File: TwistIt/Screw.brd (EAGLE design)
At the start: 33.5 x 36.5 mm, 8 parts

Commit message: Minor fixes everywhere
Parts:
- R1, R2, R3: value (none) -> 330
- ST1: value 5PIN_SCREW -> (none)
- renumbered U$1 to APM, U$2 to ST1
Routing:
- net VCC: track 16.5 -> 15.3 mm
- net P1: track 20.5 -> 19.7 mm
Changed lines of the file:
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@@
 <elements>
 <element name="JP1" library="jumper" package="JP1" value="" x="22.11928125" y="31.597309375"/>
-<element name="R1" library="resistor" package="R0603" value="" x="25.66984375" y="32.243665625" rot="R90"/>
-<element name="R2" library="resistor" package="R0603" value="" x="28.647703125" y="32.22621875" rot="R90"/>
-<element name="R3" library="resistor" package="R0603" value="" x="31.33979375" y="32.273709375" rot="R90"/>
-<element name="U$1" library="pie" package="ARDUINO_PRO_MICRO" value="ARDUINO_PRO_MICRO" x="1.778" y="1.778"/>
-<element name="U$2" library="pie" package="5PIN_SCREW" value="5PIN_SCREW" x="28.783865625" y="28.3851625" rot="MR270"/>
+<element name="R1" library="resistor" package="R0603" value="330" x="25.66984375" y="32.243665625" rot="R90"/>
+<element name="R2" library="resistor" package="R0603" value="330" x="28.647703125" y="32.22621875" rot="R90"/>
+<element name="R3" library="resistor" package="R0603" value="330" x="31.33979375" y="32.273709375" rot="R90"/>
+<element name="APM" library="pie" package="ARDUINO_PRO_MICRO" value="ARDUINO_PRO_MICRO" x="1.778" y="1.778"/>
+<element name="ST1" library="pie" package="5PIN_SCREW" value="" x="28.783865625" y="28.3851625" rot="MR270"/>
 <element name="U$3" library="pie" package="PIE-LOGO-SMALL" value="" x="5.842" y="27.94" rot="MR0"/>
 <element name="U$4" library="pie" package="OSHW-LOGO-S" value="" x="3.302" y="33.782" rot="MR0"/>
@@
 </signal>
 <signal name="GND">
-<contactref element="U$1" pad="GND@0"/>
+<contactref element="APM" pad="GND@0"/>
 <polygon width="0.4064" layer="16">
 <vertex x="0.508" y="36.068"/>
@@
 <vertex x="33.02" y="36.068"/>
 </polygon>
-<contactref element="U$2" pad="P$5"/>
+<contactref element="ST1" pad="P$5"/>
 </signal>
 <signal name="VCC">
-<contactref element="U$2" pad="P$1"/>
+<contactref element="ST1" pad="P$1"/>
 <contactref element="JP1" pad="1"/>
-<contactref element="U$1" pad="VCC"/>
-<wire x1="18.288" y1="23.368" x2="22.11928125" y2="27.19928125" width="0.8128" layer="16"/>
+<contactref element="APM" pad="VCC"/>
+<wire x1="18.796" y1="23.876" x2="22.11928125" y2="27.19928125" width="0.8128" layer="16"/>
 <wire x1="22.11928125" y1="27.19928125" x2="22.11928125" y2="30.327309375" width="0.8128" layer="16"/>
 <wire x1="25.483865625" y1="25.2851625" x2="23.566703125" y2="23.368" width="0.8128" layer="16"/>
-<wire x1="23.566703125" y1="23.368" x2="18.288" y2="23.368" width="0.8128" layer="16"/>
+<wire x1="23.566703125" y1="23.368" x2="18.796" y2="23.876" width="0.8128" layer="16"/>
 </signal>
 <signal name="P1">
 <contactref element="R1" pad="1"/>
-<contactref element="U$2" pad="P$2"/>
-<contactref element="U$1" pad="A2"/>
-<wire x1="18.288" y1="18.288" x2="20.2851625" y2="20.2851625" width="0.4064" layer="1"/>
+<contactref element="ST1" pad="P$2"/>
+<contactref element="APM" pad="A2"/>
+<wire x1="18.796" y1="18.796" x2="20.2851625" y2="20.2851625" width="0.4064" layer="1"/>
 <wire x1="20.2851625" y1="20.2851625" x2="25.483865625" y2="20.2851625" width="0.4064" layer="1"/>
 <wire x1="25.483865625" y1="20.2851625" x2="27.178" y2="21.979296875" width="0.4064" layer="1"/>
@@
 </signal>
 <signal name="P2">
-<contactref element="U$2" pad="P$3"/>
-<contactref element="U$1" pad="A1"/>
+<contactref element="ST1" pad="P$3"/>
+<contactref element="APM" pad="A1"/>
 <contactref element="R2" pad="1"/>
 <wire x1="25.483865625" y1="15.2851625" x2="28.647703125" y2="18.449" width="0.4064" layer="1"/>
 <wire x1="28.647703125" y1="18.449" x2="28.647703125" y2="31.37621875" width="0.4064" layer="1"/>
 <wire x1="25.483865625" y1="15.2851625" x2="25.021028125" y2="15.748" width="0.4064" layer="1"/>
-<wire x1="25.021028125" y1="15.748" x2="18.288" y2="15.748" width="0.4064" layer="1"/>
+<wire x1="25.021028125" y1="15.748" x2="18.796" y2="16.256" width="0.4064" layer="1"/>
 </signal>
 <signal name="P3">
-<contactref element="U$2" pad="P$4"/>
-<contactref element="U$1" pad="A0"/>
+<contactref element="ST1" pad="P$4"/>
+<contactref element="APM" pad="A0"/>
 <contactref element="R3" pad="1"/>
 <wire x1="25.483865625" y1="10.2851625" x2="22.561028125" y2="13.208" width="0.4064" layer="1"/>
-<wire x1="22.561028125" y1="13.208" x2="18.288" y2="13.208" width="0.4064" layer="1"/>
+<wire x1="22.561028125" y1="13.208" x2="18.796" y2="13.716" width="0.4064" layer="1"/>
 <wire x1="25.483865625" y1="10.2851625" x2="31.33979375" y2="16.141090625" width="0.4064" layer="1"/>
 <wire x1="31.33979375" y1="16.141090625" x2="31.33979375" y2="31.423709375" width="0.4064" layer="1"/>

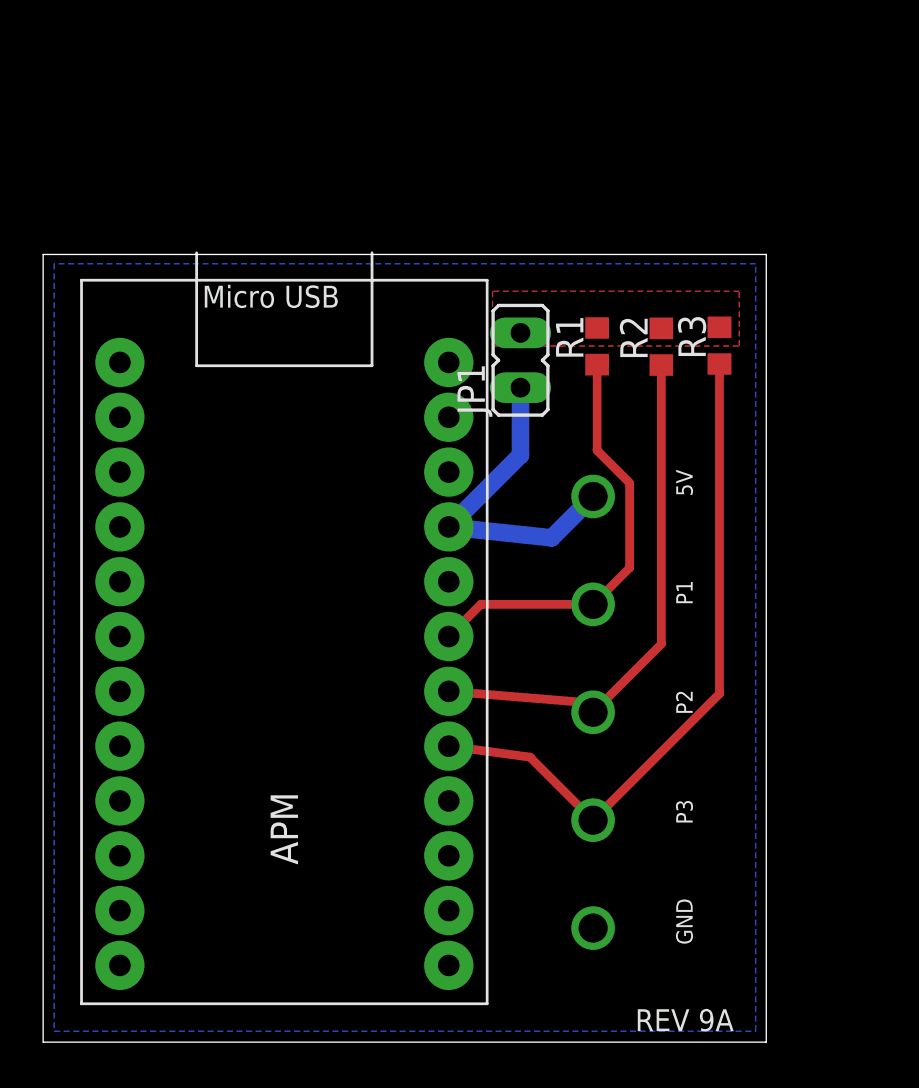
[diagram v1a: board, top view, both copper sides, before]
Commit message: Arrange TwistIt to be smaller with all components under arduino
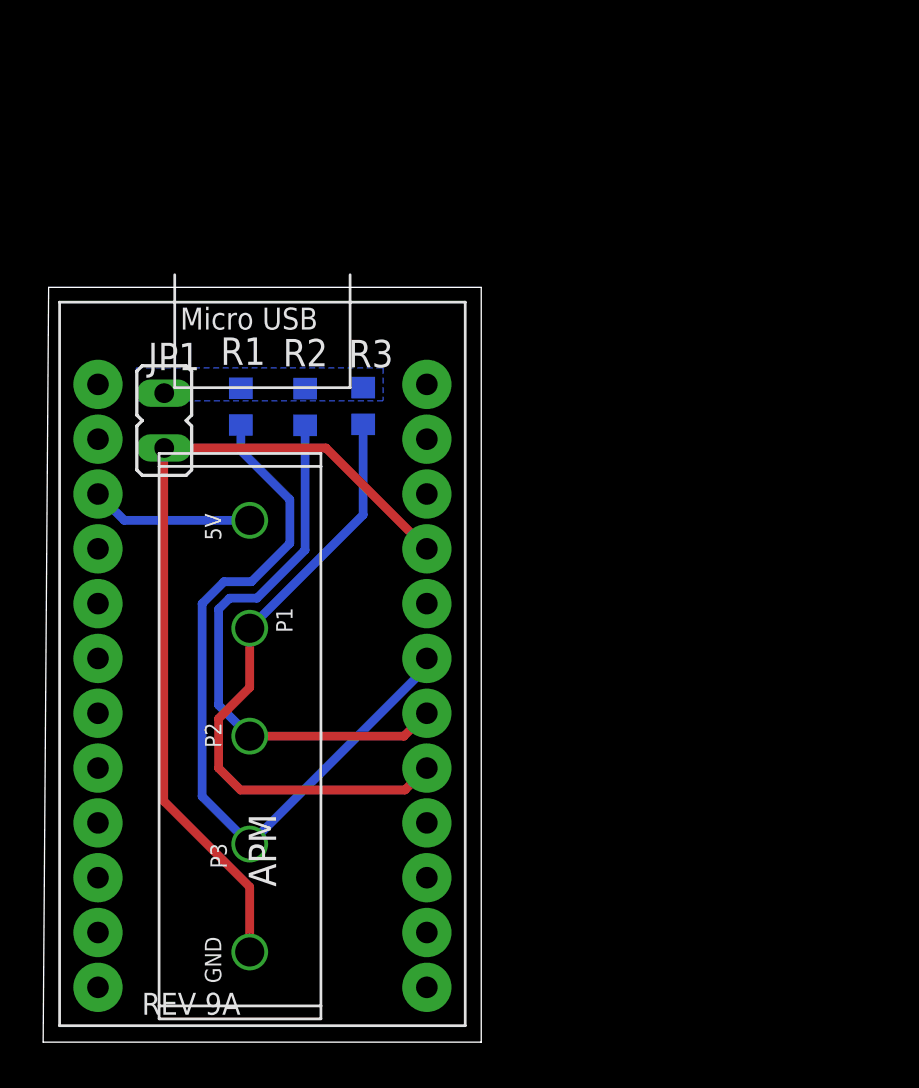
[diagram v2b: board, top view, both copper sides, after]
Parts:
- moved ST1 31.6 mm to (12.9, 1.08), flipped to the top, turned to 90 degrees
- moved JP1 16.7 mm to (5.61, 28.8)
- moved R1 16.7 mm to (9.16, 29.4), flipped to the bottom
- moved R2 16.7 mm to (12.1, 29.4), flipped to the bottom
- moved R3 16.7 mm to (14.8, 29.5), flipped to the bottom
- moved U$3 9.57 mm to (9.40, 19.1)
- moved APM 1.44 mm to (0.76, 0.76)
- moved U$4 1.44 mm to (2.29, 32.8)
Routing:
- net VCC: track 15.3 -> 39.1 mm
- net P1: track 19.7 -> 35.7 mm
- net GND: track 0.00 -> 7.54 mm
- net P3: track 31.5 -> 29.2 mm
- net P2: track 24.3 -> 26.1 mm
- added copper zone on layer 16, net 5V
- removed copper zone on layer 1, net 5V
- removed copper zone on layer 16, net GND
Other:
- board size 33.5 x 36.5 mm -> 20.3 x 35 mm

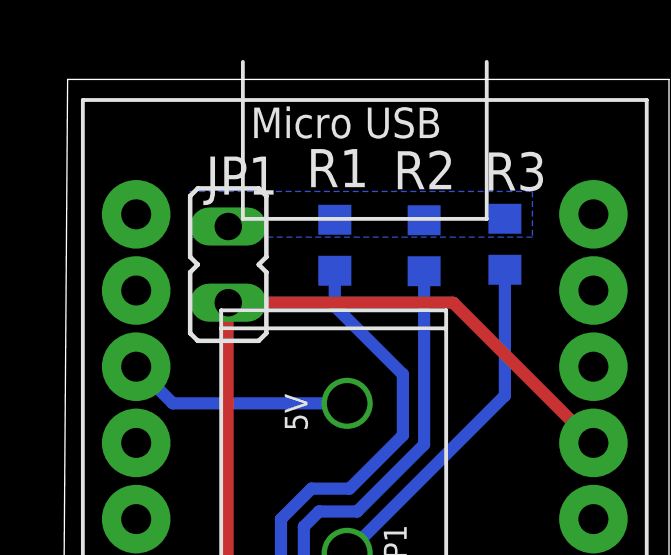
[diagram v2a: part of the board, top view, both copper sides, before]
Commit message: Mirror jumper in Screw.brd
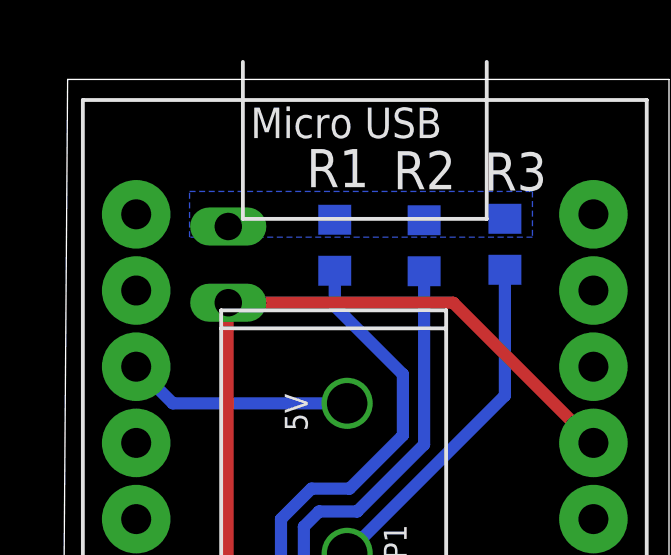
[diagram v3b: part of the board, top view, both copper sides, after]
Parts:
- flipped JP1 to the bottom
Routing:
- net VCC: vias 0 -> 1
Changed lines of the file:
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@@
 </autorouter>
 <elements>
-<element name="JP1" library="jumper" package="JP1" value="" x="5.60928125" y="28.803309375" smashed="yes">
-<attribute name="NAME" x="7.264690625" y="32.40628125" size="1.27" layer="25" font="vector" ratio="10" rot="R180"/>
-<attribute name="VALUE" x="8.53028125" y="26.263309375" size="1.27" layer="27" ratio="10" rot="R90"/>
+<element name="JP1" library="jumper" package="JP1" value="" x="5.60928125" y="28.803309375" smashed="yes" rot="MR0">
+<attribute name="NAME" x="3.953871875" y="32.40628125" size="1.27" layer="26" font="vector" ratio="10" rot="MR180"/>
+<attribute name="VALUE" x="2.68828125" y="26.263309375" size="1.27" layer="28" ratio="10" rot="MR90"/>
 </element>
 <element name="R1" library="resistor" package="R0603" value="330" x="9.15984375" y="29.449665625" smashed="yes" rot="MR90">
@@
 <wire x1="9.572134375" y1="7.191865625" x2="5.588" y2="11.176" width="0.4064" layer="1"/>
 <wire x1="5.588" y1="11.176" x2="5.588" y2="27.512028125" width="0.4064" layer="1"/>
-<wire x1="5.588" y1="27.512028125" x2="5.60928125" y2="27.533309375" width="0.4064" layer="1"/>
+<wire x1="5.588" y1="27.512028125" x2="5.60928125" y2="27.533309375" width="0.4064" layer="16"/>
+<via x="5.588" y="27.512028125" extent="1-16" drill="0.6" shape="square"/>
 </signal>
 <signal name="P1">

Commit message: Add files via upload
Mounting Holes Issue #5
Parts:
- added U$1, U$2, U$5, U$6: (no value), pie:STAND-OFF
- moved U$3 9.15 mm to (18.5, 18.8)
- moved APM 9.15 mm to (9.91, 0.51)
- moved JP1 9.15 mm to (14.8, 28.5)
- moved R2 9.15 mm to (21.3, 29.2)
- moved ST1 9.15 mm to (22.0, 0.82)
- moved U$4 9.15 mm to (11.4, 32.5)
- moved R1 9.15 mm to (18.3, 29.2)
- moved R3 9.15 mm to (24.0, 29.2)
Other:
- board size 20.3 x 35 mm -> 38.6 x 35 mm

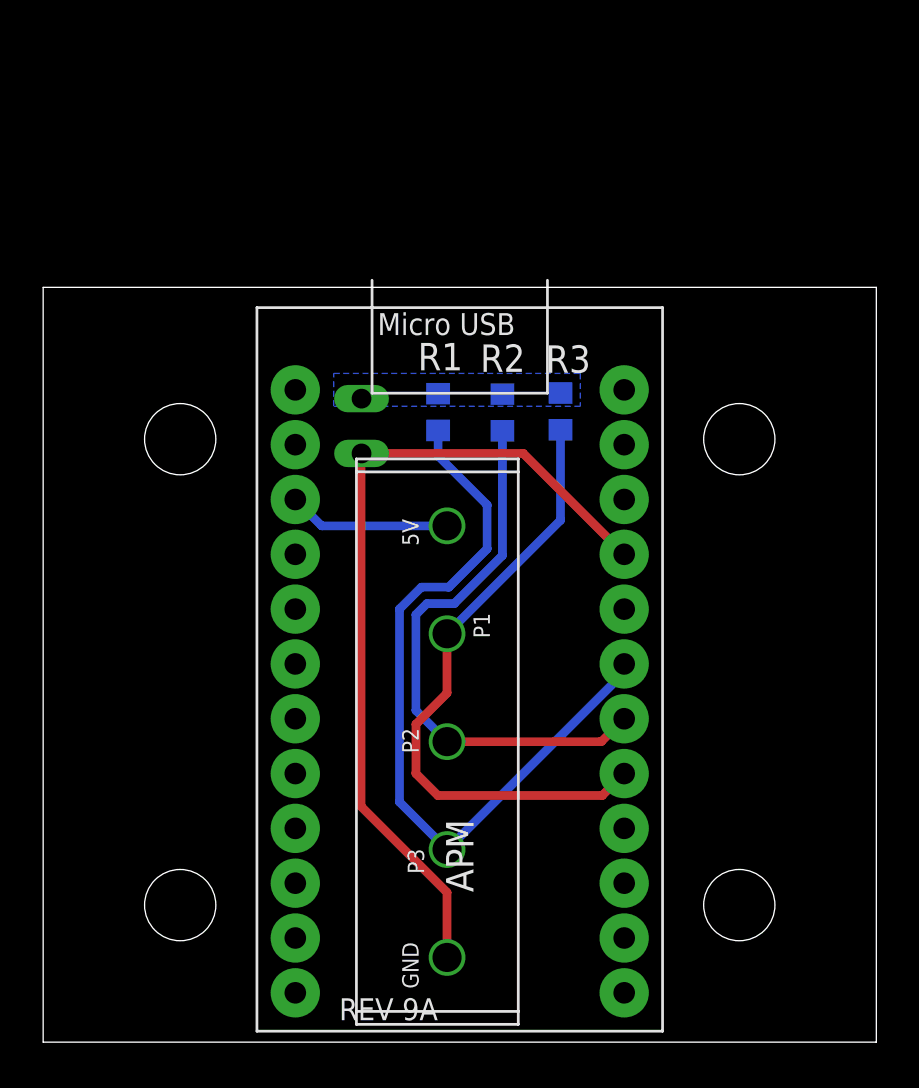
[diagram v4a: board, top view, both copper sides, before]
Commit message: Add screw terminals and names; change orientation to be ergonomic
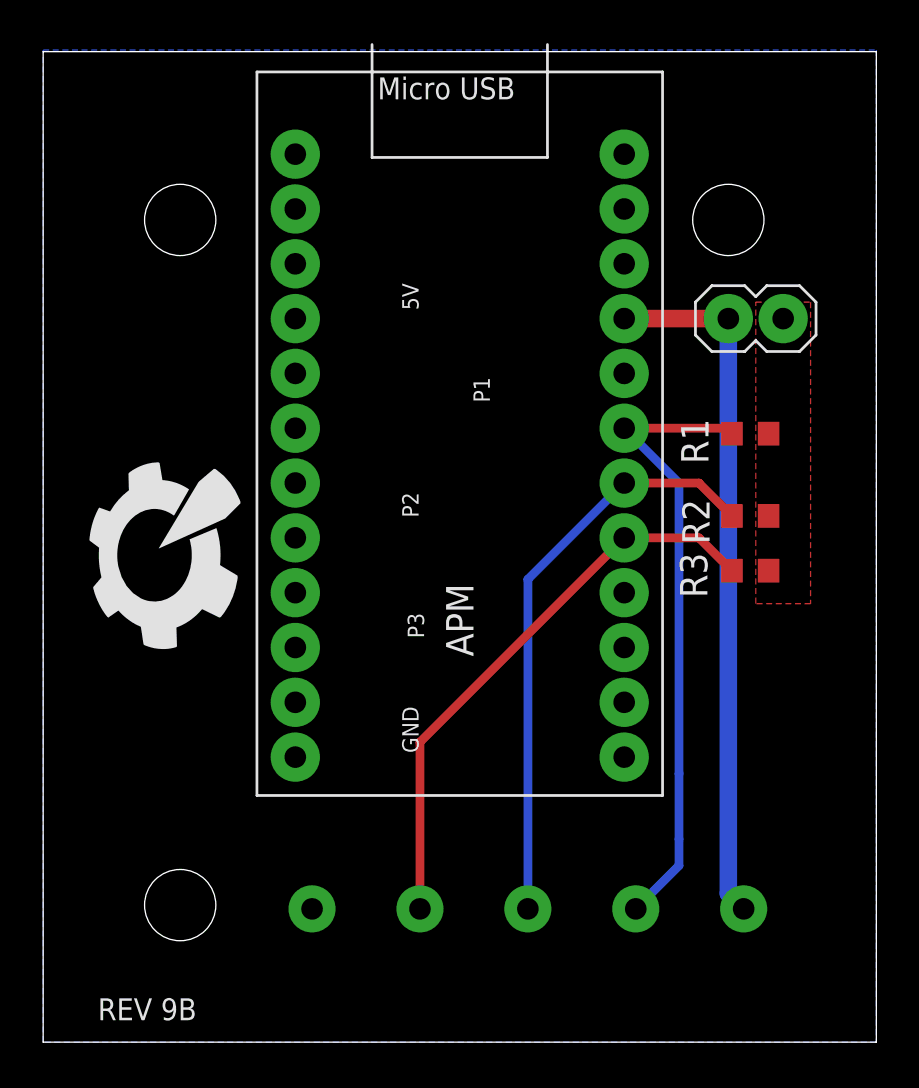
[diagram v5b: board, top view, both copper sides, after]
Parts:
- removed JP1: (no value), jumper:JP1
- removed U$2: (no value), pie:STAND-OFF
- added 5V_JUMPER: JUMPER, pie:JUMPER
- R1, R2, R3: value 330 -> 10K
- moved U$4 25.9 mm to (32.5, 17.5)
- moved R1 14.5 mm to (32.8, 28.2), flipped to the top, turned to 0 degrees
- moved U$3 13.8 mm to (5.33, 22.9), flipped to the top, turned to 90 degrees
- moved ST1 13.7 mm to (35.6, 2.88), flipped to the bottom, turned to 0 degrees
- moved R2 12.4 mm to (32.8, 24.4), flipped to the top, turned to 0 degrees
- moved R3 11.5 mm to (32.8, 21.8), flipped to the top, turned to 0 degrees
- moved APM 10.9 mm to (9.91, 11.4)
- moved U$1 10.2 mm to (31.8, 38.1)
- moved U$5 10.2 mm to (6.35, 38.1)
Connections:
- net 5V: now also 5V_JUMPER.P$2; no longer JP1.2
- net GND: now also APM.GND@1, APM.GND@2
- net VCC: now also 5V_JUMPER.P$1; no longer JP1.1
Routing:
- net GND: track 7.54 -> 0.00 mm
- net VCC: track 39.1 -> 32.5 mm, vias 1 -> 0
- net P1: track 35.7 -> 29.3 mm
- net P3: track 29.2 -> 26.7 mm
- net P2: track 26.1 -> 27.2 mm
- added copper zone on layer 1, net 5V
- added copper zone on layer 16, net GND
- removed copper zone on layer 16, net 5V
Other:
- board size 38.6 x 35 mm -> 38.6 x 45.9 mm
- board text added: "(c) Pioneers In Engineering Design by: Mohammed Hossain, Seiya Ono, Jillian Heng This design is open source hardware. For more information, visit pioneers.berkeley.edu/opensource"
- board text added: "REV 9B"
- board text removed: "(c) Pioneers In Engineering Design by: Mohammed Hossain, Seiya Ono This design is open source hardware. For more information, visit pioneers.berkeley.edu/opensource"
- board text removed: "REV 9A"
